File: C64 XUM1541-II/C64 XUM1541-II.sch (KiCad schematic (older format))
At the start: 14 parts, among them J1 C64_IEC, J2 SpeedDOS, SW1 RESET, U1 7406

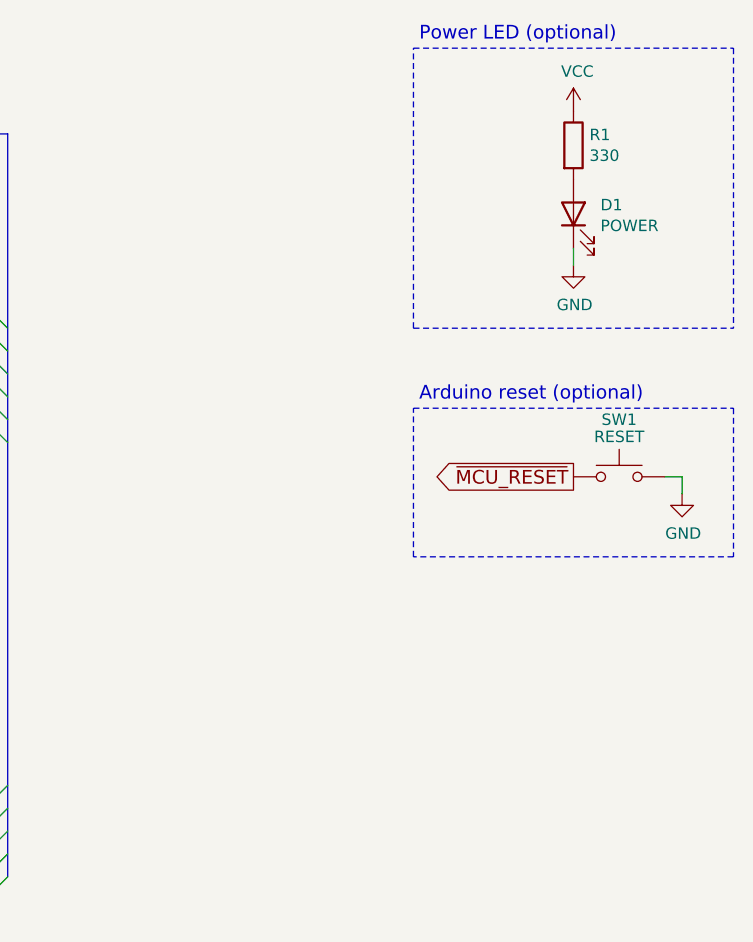
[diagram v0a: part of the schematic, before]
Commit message: User port adapter added
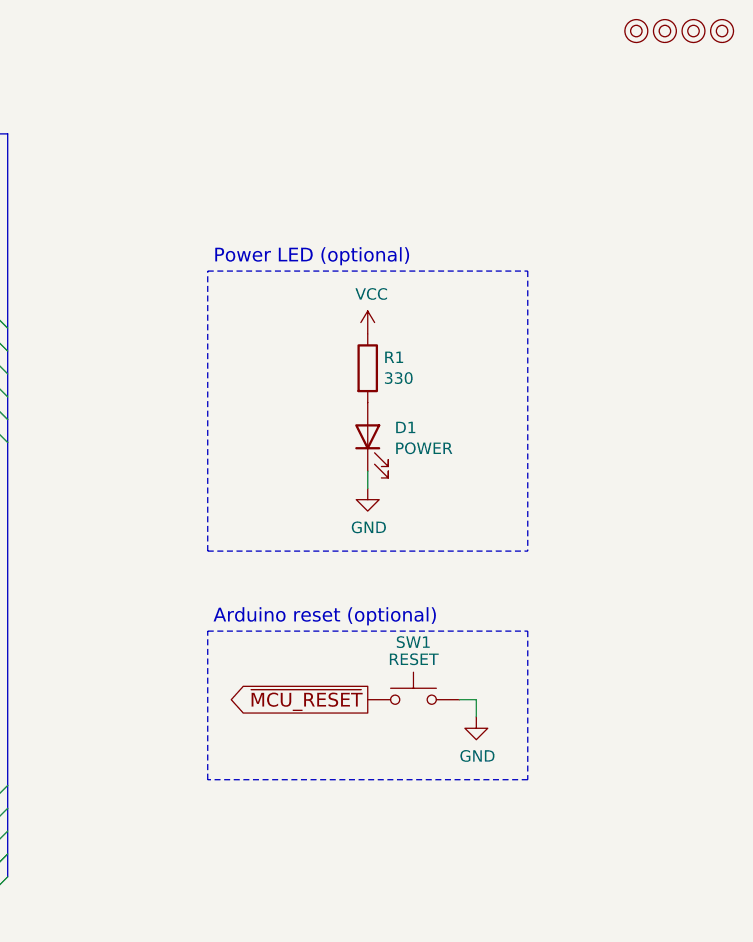
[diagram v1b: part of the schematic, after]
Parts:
- added M1, M2, M3, M4: Mounting, mounting:M3_pin, symbol mounting:Mounting
- C1: footprint (none) -> Capacitor_THT:C_Disc_D4.7mm_W2.5mm_P5.00mm
- J2: footprint Connector_IDC:IDC-Header_2x10_P2.54mm_Vertical -> speed_dos:SpeedDOS_IDC
- R1: footprint Resistors_THT:R_Axial_DIN0207_L6.3mm_D2.5mm_P10.16mm_Horizontal -> Resistor_THT:R_Axial_DIN0207_L6.3mm_D2.5mm_P10.16mm_Horizontal
- R2, R3, R4, R5, R6, R7: footprint (none) -> Resistor_THT:R_Axial_DIN0207_L6.3mm_D2.5mm_P10.16mm_Horizontal
- SW1: footprint Buttons_Switches_THT:SW_Tactile_SPST_Angled_PTS645Vx39-2LFS -> switch_cutout:SW_PUSH_6mm
- U1: footprint (none) -> Package_DIP:DIP-14_W7.62mm_Socket_LongPads
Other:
- moved on the sheet: D1, R1, SW1
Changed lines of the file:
@@
 L Device:R R1
 U 1 1 5EE0FE5F
-P 10400 1050
-F 0 "R1" H 10470 1096 50  0000 L CNN
-F 1 "330" H 10470 1005 50  0000 L CNN
-F 2 "Resistors_THT:R_Axial_DIN0207_L6.3mm_D2.5mm_P10.16mm_Horizontal" V 10330 1050 50  0001 C CNN
-F 3 "~" H 10400 1050 50  0001 C CNN
-	1    10400 1050
+P 9500 2025
+F 0 "R1" H 9570 2071 50  0000 L CNN
+F 1 "330" H 9570 1980 50  0000 L CNN
+F 2 "Resistor_THT:R_Axial_DIN0207_L6.3mm_D2.5mm_P10.16mm_Horizontal" V 9430 2025 50  0001 C CNN
+F 3 "~" H 9500 2025 50  0001 C CNN
+	1    9500 2025
 	1    0    0    -1
 $EndComp
@@
 L Device:LED D1
 U 1 1 5EE10306
-P 10400 1350
-F 0 "D1" V 10439 1232 50  0000 R CNN
-F 1 "POWER" V 10348 1232 50  0000 R CNN
-F 2 "LEDs:LED_D5.0mm" H 10400 1350 50  0001 C CNN
-F 3 "~" H 10400 1350 50  0001 C CNN
-	1    10400 1350
+P 9500 2325
+F 0 "D1" V 9539 2207 50  0000 R CNN
+F 1 "POWER" V 9448 2207 50  0000 R CNN
+F 2 "LEDs:LED_D5.0mm" H 9500 2325 50  0001 C CNN
+F 3 "~" H 9500 2325 50  0001 C CNN
+	1    9500 2325
 	0    -1   -1   0
 $EndComp
@@
 L power:VCC #PWR0103
 U 1 1 5EE10D8F
-P 10400 900
-F 0 "#PWR0103" H 10400 750 50  0001 C CNN
-F 1 "VCC" H 10417 1073 50  0000 C CNN
-F 2 "" H 10400 900 50  0001 C CNN
-F 3 "" H 10400 900 50  0001 C CNN
-	1    10400 900
+P 9500 1875
+F 0 "#PWR0103" H 9500 1725 50  0001 C CNN
+F 1 "VCC" H 9517 2048 50  0000 C CNN
+F 2 "" H 9500 1875 50  0001 C CNN
+F 3 "" H 9500 1875 50  0001 C CNN
+	1    9500 1875
 	1    0    0    -1
 $EndComp
@@
 L power:GND #PWR0104
 U 1 1 5EE111F9
-P 10400 1575
-F 0 "#PWR0104" H 10400 1325 50  0001 C CNN
-F 1 "GND" H 10405 1402 50  0000 C CNN
-F 2 "" H 10400 1575 50  0001 C CNN
-F 3 "" H 10400 1575 50  0001 C CNN
-	1    10400 1575
-	1    0    0    -1
-$EndComp
-Wire Wire Line
-	10400 1575 10400 1500
+P 9500 2550
+F 0 "#PWR0104" H 9500 2300 50  0001 C CNN
+F 1 "GND" H 9505 2377 50  0000 C CNN
+F 2 "" H 9500 2550 50  0001 C CNN
+F 3 "" H 9500 2550 50  0001 C CNN
+	1    9500 2550
+	1    0    0    -1
+$EndComp
+Wire Wire Line
+	9500 2550 9500 2475
 $Comp
 L Switch:SW_Push SW1
 U 1 1 5EE1232D
-P 10600 2500
-F 0 "SW1" H 10600 2750 50  0000 C CNN
-F 1 "RESET" H 10600 2675 50  0000 C CNN
-F 2 "Buttons_Switches_THT:SW_Tactile_SPST_Angled_PTS645Vx39-2LFS" H 10600 2700 50  0001 C CNN
-F 3 "~" H 10600 2700 50  0001 C CNN
-	1    10600 2500
+P 9700 3475
+F 0 "SW1" H 9700 3725 50  0000 C CNN
+F 1 "RESET" H 9700 3650 50  0000 C CNN
+F 2 "switch_cutout:SW_PUSH_6mm" H 9700 3675 50  0001 C CNN
+F 3 "~" H 9700 3675 50  0001 C CNN
+	1    9700 3475
 	1    0    0    -1
 $EndComp
@@
 L power:GND #PWR0105
 U 1 1 5EE13E2C
-P 10875 2575
-F 0 "#PWR0105" H 10875 2325 50  0001 C CNN
-F 1 "GND" H 10880 2402 50  0000 C CNN
-F 2 "" H 10875 2575 50  0001 C CNN
-F 3 "" H 10875 2575 50  0001 C CNN
-	1    10875 2575
-	1    0    0    -1
-$EndComp
-Wire Wire Line
-	10875 2575 10875 2500
-Wire Wire Line
-	10800 2500 10875 2500
+P 9975 3550
+F 0 "#PWR0105" H 9975 3300 50  0001 C CNN
+F 1 "GND" H 9980 3377 50  0000 C CNN
+F 2 "" H 9975 3550 50  0001 C CNN
+F 3 "" H 9975 3550 50  0001 C CNN
+	1    9975 3550
+	1    0    0    -1
+$EndComp
+Wire Wire Line
+	9975 3550 9975 3475
+Wire Wire Line
+	9900 3475 9975 3475
 Text Label 1825 2125 0    60   ~ 0
 DATA3
@@
 F 0 "J2" H 2850 5500 50  0000 C CNN
 F 1 "SpeedDOS" H 2850 5400 50  0000 C CNN
-F 2 "Connector_IDC:IDC-Header_2x10_P2.54mm_Vertical" H 2850 5075 50  0001 C CNN
+F 2 "speed_dos:SpeedDOS_IDC" H 2850 5075 50  0001 C CNN
 F 3 "~" H 2850 5075 50  0001 C CNN
 	1    2850 5075
@@
 	3725 6175 1575 6175
 Wire Notes Line
-	11100 625  11100 1850
-Text Notes 9725 600  0    60   ~ 0
+	10200 1600 10200 2825
+Text Notes 8825 1575 0    60   ~ 0
 Power LED (optional)
 Text Notes 1775 4525 0    60   ~ 0
@@
 F 0 "U1" H 6337 2362 60  0000 C CNN
 F 1 "7406" H 6337 2256 60  0000 C CNN
-F 2 "" H 6450 1875 60  0001 C CNN
+F 2 "Package_DIP:DIP-14_W7.62mm_Socket_LongPads" H 6450 1875 60  0001 C CNN
 F 3 "" H 6450 1875 60  0001 C CNN
 	1    6325 1850
@@
 F 0 "R4" V 5750 2325 50  0000 L CNN
 F 1 "100k" V 5750 2475 50  0000 L CNN
-F 2 "" H 5675 2475 50  0001 C CNN
+F 2 "Resistor_THT:R_Axial_DIN0207_L6.3mm_D2.5mm_P10.16mm_Horizontal" H 5675 2475 50  0001 C CNN
 F 3 "~" H 5675 2475 50  0001 C CNN
 	1    5675 2475
@@
 F 0 "R3" V 5600 2325 50  0000 L CNN
 F 1 "100k" V 5600 2475 50  0000 L CNN
-F 2 "" H 5525 2475 50  0001 C CNN
+F 2 "Resistor_THT:R_Axial_DIN0207_L6.3mm_D2.5mm_P10.16mm_Horizontal" H 5525 2475 50  0001 C CNN
 F 3 "~" H 5525 2475 50  0001 C CNN
 	1    5525 2475
@@
 F 0 "R2" V 5450 2325 50  0000 L CNN
 F 1 "100k" V 5450 2475 50  0000 L CNN
-F 2 "" H 5375 2475 50  0001 C CNN
+F 2 "Resistor_THT:R_Axial_DIN0207_L6.3mm_D2.5mm_P10.16mm_Horizontal" H 5375 2475 50  0001 C CNN
 F 3 "~" H 5375 2475 50  0001 C CNN
 	1    5375 2475
@@
 F 0 "R5" V 6950 2325 50  0000 L CNN
 F 1 "100k" V 6950 2475 50  0000 L CNN
-F 2 "" H 6875 2475 50  0001 C CNN
+F 2 "Resistor_THT:R_Axial_DIN0207_L6.3mm_D2.5mm_P10.16mm_Horizontal" H 6875 2475 50  0001 C CNN
 F 3 "~" H 6875 2475 50  0001 C CNN
 	1    6875 2475
@@
 F 0 "R6" V 7100 2325 50  0000 L CNN
 F 1 "100k" V 7100 2475 50  0000 L CNN
-F 2 "" H 7025 2475 50  0001 C CNN
+F 2 "Resistor_THT:R_Axial_DIN0207_L6.3mm_D2.5mm_P10.16mm_Horizontal" H 7025 2475 50  0001 C CNN
 F 3 "~" H 7025 2475 50  0001 C CNN
 	1    7025 2475
@@
 F 0 "R7" V 7250 2325 50  0000 L CNN
 F 1 "100k" V 7250 2475 50  0000 L CNN
-F 2 "" H 7175 2475 50  0001 C CNN
+F 2 "Resistor_THT:R_Axial_DIN0207_L6.3mm_D2.5mm_P10.16mm_Horizontal" H 7175 2475 50  0001 C CNN
 F 3 "~" H 7175 2475 50  0001 C CNN
 	1    7175 2475
@@
 F 0 "C1" H 6567 7296 50  0000 L CNN
 F 1 "100nF" H 6567 7205 50  0000 L CNN
-F 2 "" H 6475 7250 50  0001 C CNN
+F 2 "Capacitor_THT:C_Disc_D4.7mm_W2.5mm_P5.00mm" H 6475 7250 50  0001 C CNN
 F 3 "~" H 6475 7250 50  0001 C CNN
 	1    6475 7250
@@
 Wire Wire Line
 	6725 4350 7825 4350
-Text GLabel 10400 2500 0    60   Output ~ 0
+Text GLabel 9500 3475 0    60   Output ~ 0
 ~MCU_RESET
 Text GLabel 3250 2325 2    60   Input ~ 0
 ~MCU_RESET
 Wire Notes Line
-	11100 2200 11100 2850
-Wire Notes Line
-	11100 2850 9700 2850
-Wire Notes Line
-	9700 2850 9700 2200
-Wire Notes Line
-	9700 2200 11100 2200
-Wire Notes Line
-	9700 1850 9700 625
-Wire Notes Line
-	9700 625  11100 625
-Wire Notes Line
-	9700 1850 11100 1850
-Text Notes 9725 2175 0    60   ~ 0
+	10200 3175 10200 3825
+Wire Notes Line
+	10200 3825 8800 3825
+Wire Notes Line
+	8800 3825 8800 3175
+Wire Notes Line
+	8800 3175 10200 3175
+Wire Notes Line
+	8800 2825 8800 1600
+Wire Notes Line
+	8800 1600 10200 1600
+Wire Notes Line
+	8800 2825 10200 2825
+Text Notes 8825 3150 0    60   ~ 0
 Arduino reset (optional)
 Wire Bus Line
@@
 Wire Bus Line
 	3850 1000 4750 1000
+$Comp
+L mounting:Mounting M1
+U 1 1 6049C1C8
+P 10675 550
+F 0 "M1" H 10675 650 50  0001 C CNN
+F 1 "Mounting" H 10675 475 50  0001 C CNN
+F 2 "mounting:M3_pin" H 10675 550 50  0001 C CNN
+F 3 "~" H 10675 550 50  0001 C CNN
+	1    10675 550
+	1    0    0    -1
+$EndComp
+$Comp
+L mounting:Mounting M2
+U 1 1 6049C9D2
+P 10800 550
+F 0 "M2" H 10800 650 50  0001 C CNN
+F 1 "Mounting" H 10800 475 50  0001 C CNN
+F 2 "mounting:M3_pin" H 10800 550 50  0001 C CNN
+F 3 "~" H 10800 550 50  0001 C CNN
+	1    10800 550
+	1    0    0    -1
+$EndComp
+$Comp
+L mounting:Mounting M3
+U 1 1 6049F898
+P 10925 550
+F 0 "M3" H 10925 650 50  0001 C CNN
+F 1 "Mounting" H 10925 475 50  0001 C CNN
+F 2 "mounting:M3_pin" H 10925 550 50  0001 C CNN
+F 3 "~" H 10925 550 50  0001 C CNN
+	1    10925 550
+	1    0    0    -1
+$EndComp
+$Comp
+L mounting:Mounting M4
+U 1 1 604A26DE
+P 11050 550
+F 0 "M4" H 11050 650 50  0001 C CNN
+F 1 "Mounting" H 11050 475 50  0001 C CNN
+F 2 "mounting:M3_pin" H 11050 550 50  0001 C CNN
+F 3 "~" H 11050 550 50  0001 C CNN
+	1    11050 550
+	1    0    0    -1
+$EndComp
 Wire Bus Line
 	4750 1000 4750 2050

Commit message: First new layout draft
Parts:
- removed R4: 100k, Resistor_THT:R_Axial_DIN0207_L6.3mm_D2.5mm_P10.16mm_Horizontal, symbol Device:R_Small
- added D2: ACTIVITY, LED_THT:LED_D5.0mm, symbol Device:LED
- added R4: 330, Resistor_THT:R_Axial_DIN0207_L6.3mm_D2.5mm_P10.16mm_Horizontal, symbol Device:R
- D1: footprint LEDs:LED_D5.0mm -> LED_THT:LED_D5.0mm
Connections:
- net CLK: now also U1.1 (1A)
- net VCC: now also R4.1
- net ACT: now reaches U1.2 (1Y)
- net ACT: now also D2.1 (K)
- new net: D2.2 (A), R4.2
- no-connect marks 4 -> 3
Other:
- note added: "LED indicators (optional)"
- note removed: "Power LED (optional)"
- moved on the sheet: D1, R1
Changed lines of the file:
@@
 L Device:R R1
 U 1 1 5EE0FE5F
-P 9500 2025
-F 0 "R1" H 9570 2071 50  0000 L CNN
-F 1 "330" H 9570 1980 50  0000 L CNN
-F 2 "Resistor_THT:R_Axial_DIN0207_L6.3mm_D2.5mm_P10.16mm_Horizontal" V 9430 2025 50  0001 C CNN
-F 3 "~" H 9500 2025 50  0001 C CNN
-	1    9500 2025
+P 9000 2025
+F 0 "R1" H 9070 2071 50  0000 L CNN
+F 1 "330" H 9070 1980 50  0000 L CNN
+F 2 "Resistor_THT:R_Axial_DIN0207_L6.3mm_D2.5mm_P10.16mm_Horizontal" V 8930 2025 50  0001 C CNN
+F 3 "~" H 9000 2025 50  0001 C CNN
+	1    9000 2025
 	1    0    0    -1
 $EndComp
@@
 L Device:LED D1
 U 1 1 5EE10306
-P 9500 2325
-F 0 "D1" V 9539 2207 50  0000 R CNN
-F 1 "POWER" V 9448 2207 50  0000 R CNN
-F 2 "LEDs:LED_D5.0mm" H 9500 2325 50  0001 C CNN
-F 3 "~" H 9500 2325 50  0001 C CNN
-	1    9500 2325
+P 9000 2325
+F 0 "D1" V 9039 2207 50  0000 R CNN
+F 1 "POWER" V 8948 2207 50  0000 R CNN
+F 2 "LED_THT:LED_D5.0mm" H 9000 2325 50  0001 C CNN
+F 3 "~" H 9000 2325 50  0001 C CNN
+	1    9000 2325
 	0    -1   -1   0
 $EndComp
@@
 L power:VCC #PWR0103
 U 1 1 5EE10D8F
-P 9500 1875
-F 0 "#PWR0103" H 9500 1725 50  0001 C CNN
-F 1 "VCC" H 9517 2048 50  0000 C CNN
-F 2 "" H 9500 1875 50  0001 C CNN
-F 3 "" H 9500 1875 50  0001 C CNN
-	1    9500 1875
+P 9000 1875
+F 0 "#PWR0103" H 9000 1725 50  0001 C CNN
+F 1 "VCC" H 9017 2048 50  0000 C CNN
+F 2 "" H 9000 1875 50  0001 C CNN
+F 3 "" H 9000 1875 50  0001 C CNN
+	1    9000 1875
 	1    0    0    -1
 $EndComp
@@
 L power:GND #PWR0104
 U 1 1 5EE111F9
-P 9500 2550
-F 0 "#PWR0104" H 9500 2300 50  0001 C CNN
-F 1 "GND" H 9505 2377 50  0000 C CNN
-F 2 "" H 9500 2550 50  0001 C CNN
-F 3 "" H 9500 2550 50  0001 C CNN
-	1    9500 2550
-	1    0    0    -1
-$EndComp
-Wire Wire Line
-	9500 2550 9500 2475
+P 9000 2550
+F 0 "#PWR0104" H 9000 2300 50  0001 C CNN
+F 1 "GND" H 9005 2377 50  0000 C CNN
+F 2 "" H 9000 2550 50  0001 C CNN
+F 3 "" H 9000 2550 50  0001 C CNN
+	1    9000 2550
+	1    0    0    -1
+$EndComp
+Wire Wire Line
+	9000 2550 9000 2475
 $Comp
 L Switch:SW_Push SW1
@@
 	10200 1600 10200 2825
 Text Notes 8825 1575 0    60   ~ 0
-Power LED (optional)
+LED indicators (optional)
 Text Notes 1775 4525 0    60   ~ 0
 Parallel cable (optional)
@@
 	1    0    0    -1
 $EndComp
-$Comp
-L Device:R_Small R4
-U 1 1 6051738B
-P 5675 2475
-F 0 "R4" V 5750 2325 50  0000 L CNN
-F 1 "100k" V 5750 2475 50  0000 L CNN
-F 2 "Resistor_THT:R_Axial_DIN0207_L6.3mm_D2.5mm_P10.16mm_Horizontal" H 5675 2475 50  0001 C CNN
-F 3 "~" H 5675 2475 50  0001 C CNN
-	1    5675 2475
-	1    0    0    -1
-$EndComp
 Wire Wire Line
 	5875 2250 5800 2250
 Wire Wire Line
 	5800 2250 5800 2650
-Wire Wire Line
-	5675 2575 5675 2650
-Wire Wire Line
-	5675 2650 5800 2650
-Wire Wire Line
-	5675 2375 5675 1650
-Wire Wire Line
-	5675 1650 5875 1650
 $Comp
 L Device:R_Small R3
@@
 Wire Wire Line
 	5525 2575 5525 2650
-Wire Wire Line
-	5525 2650 5675 2650
-Connection ~ 5675 2650
 Wire Wire Line
 	5375 2575 5375 2650
@@
 Wire Wire Line
 	6725 4525 6725 4350
-NoConn ~ 5875 1750
 Entry Wire Line
 	7925 3850 7825 3950
@@
 	1    0    0    -1
 $EndComp
+Wire Wire Line
+	5525 2650 5800 2650
+Wire Wire Line
+	5525 1850 5525 1650
+Wire Wire Line
+	5525 1650 5875 1650
+Text GLabel 5800 1750 0    60   Output ~ 0
+ACT
+Wire Wire Line
+	5875 1750 5800 1750
+$Comp
+L Device:R R4
+U 1 1 604FC955
+P 9600 2025
+F 0 "R4" H 9670 2071 50  0000 L CNN
+F 1 "330" H 9670 1980 50  0000 L CNN
+F 2 "Resistor_THT:R_Axial_DIN0207_L6.3mm_D2.5mm_P10.16mm_Horizontal" V 9530 2025 50  0001 C CNN
+F 3 "~" H 9600 2025 50  0001 C CNN
+	1    9600 2025
+	1    0    0    -1
+$EndComp
+$Comp
+L Device:LED D2
+U 1 1 604FC95B
+P 9600 2325
+F 0 "D2" V 9639 2207 50  0000 R CNN
+F 1 "ACTIVITY" V 9548 2207 50  0000 R CNN
+F 2 "LED_THT:LED_D5.0mm" H 9600 2325 50  0001 C CNN
+F 3 "~" H 9600 2325 50  0001 C CNN
+	1    9600 2325
+	0    -1   -1   0
+$EndComp
+$Comp
+L power:VCC #PWR0110
+U 1 1 604FC961
+P 9600 1875
+F 0 "#PWR0110" H 9600 1725 50  0001 C CNN
+F 1 "VCC" H 9617 2048 50  0000 C CNN
+F 2 "" H 9600 1875 50  0001 C CNN
+F 3 "" H 9600 1875 50  0001 C CNN
+	1    9600 1875
+	1    0    0    -1
+$EndComp
+Wire Wire Line
+	9600 2550 9600 2475
+Text GLabel 9600 2550 3    60   Input ~ 0
+ACT
 Wire Bus Line
 	4750 1000 4750 2050

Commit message: ACTIVITY is now DRIVE LED
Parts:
- D2: value ACTIVITY -> DRIVE
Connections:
- net ATN: now also U1.1 (1A)
- net CLK: no longer U1.1 (1A)
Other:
- moved on the sheet: R5
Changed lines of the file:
@@
 L Device:R_Small R5
 U 1 1 6052AA23
-P 6875 2475
-F 0 "R5" V 6950 2325 50  0000 L CNN
-F 1 "100k" V 6950 2475 50  0000 L CNN
-F 2 "Resistor_THT:R_Axial_DIN0207_L6.3mm_D2.5mm_P10.16mm_Horizontal" H 6875 2475 50  0001 C CNN
-F 3 "~" H 6875 2475 50  0001 C CNN
-	1    6875 2475
-	1    0    0    -1
-$EndComp
-Wire Wire Line
-	6875 2375 6875 2150
+P 7325 2475
+F 0 "R5" V 7400 2325 50  0000 L CNN
+F 1 "100k" V 7400 2475 50  0000 L CNN
+F 2 "Resistor_THT:R_Axial_DIN0207_L6.3mm_D2.5mm_P10.16mm_Horizontal" H 7325 2475 50  0001 C CNN
+F 3 "~" H 7325 2475 50  0001 C CNN
+	1    7325 2475
+	1    0    0    -1
+$EndComp
+Wire Wire Line
+	7325 2375 7325 2150
 $Comp
 L Device:R_Small R6
@@
 	7025 1950 6800 1950
 Wire Wire Line
-	6875 2650 6875 2575
-Wire Wire Line
-	6875 2650 7025 2650
+	7325 2650 7325 2575
 Wire Wire Line
 	7025 2650 7025 2575
@@
 L power:GND #PWR0106
 U 1 1 60541E11
-P 7025 2725
-F 0 "#PWR0106" H 7025 2475 50  0001 C CNN
-F 1 "GND" H 7030 2552 50  0000 C CNN
-F 2 "" H 7025 2725 50  0001 C CNN
-F 3 "" H 7025 2725 50  0001 C CNN
-	1    7025 2725
-	1    0    0    -1
-$EndComp
-Wire Wire Line
-	7025 2725 7025 2650
-Connection ~ 7025 2650
+P 7175 2725
+F 0 "#PWR0106" H 7175 2475 50  0001 C CNN
+F 1 "GND" H 7180 2552 50  0000 C CNN
+F 2 "" H 7175 2725 50  0001 C CNN
+F 3 "" H 7175 2725 50  0001 C CNN
+	1    7175 2725
+	1    0    0    -1
+$EndComp
+Wire Wire Line
+	7175 2725 7175 2650
 Wire Wire Line
 	6800 2050 7825 2050
-Wire Wire Line
-	6800 2150 6875 2150
-Connection ~ 6875 2150
-Wire Wire Line
-	6875 2150 7825 2150
 Wire Wire Line
 	6800 2250 7825 2250
@@
 Wire Wire Line
 	5525 2650 5800 2650
-Wire Wire Line
-	5525 1850 5525 1650
-Wire Wire Line
-	5525 1650 5875 1650
 Text GLabel 5800 1750 0    60   Output ~ 0
 ACT
@@
 P 9600 2325
 F 0 "D2" V 9639 2207 50  0000 R CNN
-F 1 "ACTIVITY" V 9548 2207 50  0000 R CNN
+F 1 "DRIVE" V 9548 2207 50  0000 R CNN
 F 2 "LED_THT:LED_D5.0mm" H 9600 2325 50  0001 C CNN
 F 3 "~" H 9600 2325 50  0001 C CNN
@@
 Text GLabel 9600 2550 3    60   Input ~ 0
 ACT
+Connection ~ 7325 2150
+Wire Wire Line
+	7325 2150 7825 2150
+Wire Wire Line
+	6800 2150 7325 2150
+Connection ~ 7175 2650
+Wire Wire Line
+	7175 2650 7325 2650
+Wire Wire Line
+	7325 2150 7325 1200
+Wire Wire Line
+	7325 1200 5800 1200
+Wire Wire Line
+	5800 1200 5800 1650
+Wire Wire Line
+	5800 1650 5875 1650
 Wire Bus Line
 	4750 1000 4750 2050

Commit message: Increase space for M3 nut
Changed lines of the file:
@@
 L mounting:Mounting M1
 U 1 1 6049C1C8
-P 10675 550
-F 0 "M1" H 10675 650 50  0001 C CNN
-F 1 "Mounting" H 10675 475 50  0001 C CNN
-F 2 "mounting:M3_pin" H 10675 550 50  0001 C CNN
-F 3 "~" H 10675 550 50  0001 C CNN
-	1    10675 550
+P 10725 550
+F 0 "M1" H 10725 650 50  0001 C CNN
+F 1 "Mounting" H 10725 475 50  0001 C CNN
+F 2 "mounting:M3_pin" H 10725 550 50  0001 C CNN
+F 3 "~" H 10725 550 50  0001 C CNN
+	1    10725 550
 	1    0    0    -1
 $EndComp
@@
 L mounting:Mounting M2
 U 1 1 6049C9D2
-P 10800 550
-F 0 "M2" H 10800 650 50  0001 C CNN
-F 1 "Mounting" H 10800 475 50  0001 C CNN
-F 2 "mounting:M3_pin" H 10800 550 50  0001 C CNN
-F 3 "~" H 10800 550 50  0001 C CNN
-	1    10800 550
+P 10850 550
+F 0 "M2" H 10850 650 50  0001 C CNN
+F 1 "Mounting" H 10850 475 50  0001 C CNN
+F 2 "mounting:M3_pin" H 10850 550 50  0001 C CNN
+F 3 "~" H 10850 550 50  0001 C CNN
+	1    10850 550
 	1    0    0    -1
 $EndComp
@@
 L mounting:Mounting M3
 U 1 1 6049F898
-P 10925 550
-F 0 "M3" H 10925 650 50  0001 C CNN
-F 1 "Mounting" H 10925 475 50  0001 C CNN
-F 2 "mounting:M3_pin" H 10925 550 50  0001 C CNN
-F 3 "~" H 10925 550 50  0001 C CNN
-	1    10925 550
+P 10975 550
+F 0 "M3" H 10975 650 50  0001 C CNN
+F 1 "Mounting" H 10975 475 50  0001 C CNN
+F 2 "mounting:M3_pin" H 10975 550 50  0001 C CNN
+F 3 "~" H 10975 550 50  0001 C CNN
+	1    10975 550
 	1    0    0    -1
 $EndComp
@@
 L mounting:Mounting M4
 U 1 1 604A26DE
-P 11050 550
-F 0 "M4" H 11050 650 50  0001 C CNN
-F 1 "Mounting" H 11050 475 50  0001 C CNN
-F 2 "mounting:M3_pin" H 11050 550 50  0001 C CNN
-F 3 "~" H 11050 550 50  0001 C CNN
-	1    11050 550
+P 11100 550
+F 0 "M4" H 11100 650 50  0001 C CNN
+F 1 "Mounting" H 11100 475 50  0001 C CNN
+F 2 "mounting:M3_pin" H 11100 550 50  0001 C CNN
+F 3 "~" H 11100 550 50  0001 C CNN
+	1    11100 550
 	1    0    0    -1
 $EndComp
